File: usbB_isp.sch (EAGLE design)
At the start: 12 parts, among them IC1 788TV, IC2 TINY13-20PU, X1 PN61729-S

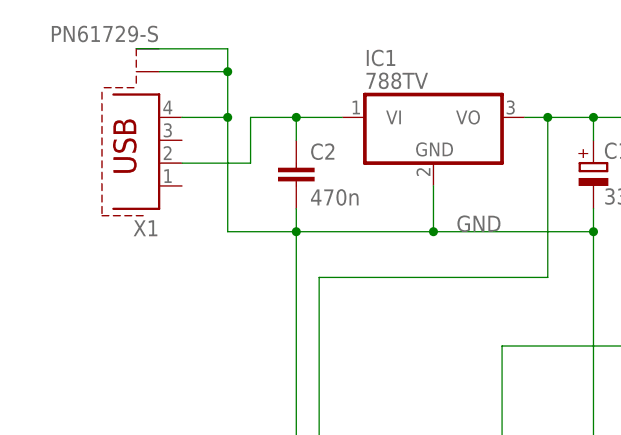
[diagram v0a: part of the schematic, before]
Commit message: fixing usb-pins
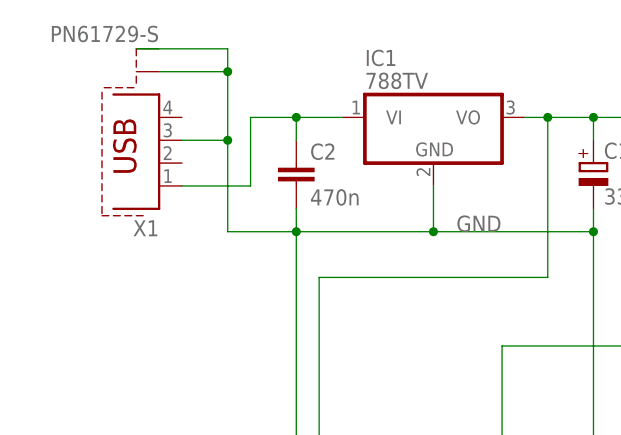
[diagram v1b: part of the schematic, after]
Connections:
- net GND: now also X1.3; no longer X1.4
- net N$1: now also X1.1; no longer X1.2
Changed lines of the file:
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@@
 </busses>
 <nets>
-<net name="N$1" class="0">
-<segment>
-<pinref part="C2" gate="G$1" pin="1"/>
-<pinref part="IC1" gate="A1" pin="VI"/>
-<wire x1="7.62" y1="71.12" x2="12.7" y2="71.12" width="0.1524" layer="91"/>
-<pinref part="X1" gate="G$1" pin="2"/>
-<wire x1="-5.08" y1="66.04" x2="2.54" y2="66.04" width="0.1524" layer="91"/>
-<wire x1="2.54" y1="66.04" x2="2.54" y2="71.12" width="0.1524" layer="91"/>
-<wire x1="2.54" y1="71.12" x2="7.62" y2="71.12" width="0.1524" layer="91"/>
-<wire x1="7.62" y1="71.12" x2="7.62" y2="68.58" width="0.1524" layer="91"/>
-<junction x="7.62" y="71.12"/>
-</segment>
-</net>
 <net name="GND" class="0">
 <segment>
@@
 <junction x="152.4" y="58.42"/>
 <wire x1="152.4" y1="48.26" x2="152.4" y2="58.42" width="0.1524" layer="91"/>
-<wire x1="0" y1="58.42" x2="0" y2="71.12" width="0.1524" layer="91"/>
-<pinref part="X1" gate="G$1" pin="4"/>
-<wire x1="0" y1="71.12" x2="-5.08" y2="71.12" width="0.1524" layer="91"/>
-<wire x1="0" y1="71.12" x2="0" y2="76.2" width="0.1524" layer="91"/>
 <pinref part="X1" gate="G$1" pin="S1"/>
 <wire x1="-7.62" y1="76.2" x2="0" y2="76.2" width="0.1524" layer="91"/>
 <wire x1="0" y1="76.2" x2="0" y2="78.74" width="0.1524" layer="91"/>
 <wire x1="0" y1="78.74" x2="-10.16" y2="78.74" width="0.1524" layer="91"/>
-<junction x="0" y="71.12"/>
 <junction x="0" y="76.2"/>
+<wire x1="0" y1="58.42" x2="0" y2="68.58" width="0.1524" layer="91"/>
+<pinref part="X1" gate="G$1" pin="3"/>
+<wire x1="0" y1="68.58" x2="0" y2="76.2" width="0.1524" layer="91"/>
+<wire x1="-5.08" y1="68.58" x2="0" y2="68.58" width="0.1524" layer="91"/>
+<junction x="0" y="68.58"/>
 </segment>
 </net>
@@
 </segment>
 </net>
+<net name="N$1" class="0">
+<segment>
+<pinref part="C2" gate="G$1" pin="1"/>
+<pinref part="IC1" gate="A1" pin="VI"/>
+<wire x1="7.62" y1="71.12" x2="12.7" y2="71.12" width="0.1524" layer="91"/>
+<wire x1="7.62" y1="71.12" x2="7.62" y2="68.58" width="0.1524" layer="91"/>
+<pinref part="X1" gate="G$1" pin="1"/>
+<wire x1="-5.08" y1="63.5" x2="2.54" y2="63.5" width="0.1524" layer="91"/>
+<wire x1="2.54" y1="63.5" x2="2.54" y2="71.12" width="0.1524" layer="91"/>
+<wire x1="2.54" y1="71.12" x2="7.62" y2="71.12" width="0.1524" layer="91"/>
+<junction x="7.62" y="71.12"/>
+</segment>
+</net>

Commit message: done stuff
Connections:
- net GND: no longer X1.3
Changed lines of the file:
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@@
 <junction x="152.4" y="58.42"/>
 <wire x1="152.4" y1="48.26" x2="152.4" y2="58.42" width="0.1524" layer="91"/>
+<wire x1="0" y1="78.74" x2="-10.16" y2="78.74" width="0.1524" layer="91"/>
 <pinref part="X1" gate="G$1" pin="S1"/>
 <wire x1="-7.62" y1="76.2" x2="0" y2="76.2" width="0.1524" layer="91"/>
 <wire x1="0" y1="76.2" x2="0" y2="78.74" width="0.1524" layer="91"/>
-<wire x1="0" y1="78.74" x2="-10.16" y2="78.74" width="0.1524" layer="91"/>
 <junction x="0" y="76.2"/>
-<wire x1="0" y1="58.42" x2="0" y2="68.58" width="0.1524" layer="91"/>
-<pinref part="X1" gate="G$1" pin="3"/>
-<wire x1="0" y1="68.58" x2="0" y2="76.2" width="0.1524" layer="91"/>
-<wire x1="-5.08" y1="68.58" x2="0" y2="68.58" width="0.1524" layer="91"/>
-<junction x="0" y="68.58"/>
+<wire x1="0" y1="76.2" x2="0" y2="58.42" width="0.1524" layer="91"/>
 </segment>
 </net>
